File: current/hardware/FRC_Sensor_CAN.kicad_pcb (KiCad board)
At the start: 4 copper layers, 52 x 74 mm, 144 parts, among them J1 2P PUSH 3.5mm, J2 2P PUSH 3.5mm, J3 2P PUSH 3.5mm, J4 3P PUSH 3.5mm, J5 3P PUSH 3.5mm, J6 3P PUSH 3.5mm, J8 2x5 SERVICE SOCKET 2.54mm, Q1 AO4485, Q101 AO3401A, Q102 BSS138BK, Q2 BSS138BK, Q201 AO3401A, Q202 BSS138BK, Q3 BSS138BK, Q301 AO3401A, Q302 BSS138BK, U1 LMR51420XDDCR, U10 SN74AHCT1G125, U2 AP2112K-3.3, U4 TPS2553DBVR-1, U5 STM32F042K6T6, U6 TCAN3413DR, U7 LM339LV, U8 TPS61085DGKR, U9 TPS259620DDAR, Y1 8MHz 18pF

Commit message: Prepare factory SMT assembly with high-reflow C1 and exact MCU sourcing
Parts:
- C1: footprint FRC_Sensor_CAN:CP_Elec_8x6.5 -> FRC_Sensor_CAN:CP_Panasonic_FT_6.3x5.8

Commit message: Improve crystal startup margin and refresh pre-order verification
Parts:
- C25, C26: value 30pF -> 20pF
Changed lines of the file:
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@@
 			)
 		)
-		(property "Value" "30pF"
+		(property "Value" "20pF"
 			(at 0 1.68 90)
 			(layer "F.Fab")
@@
 			)
 		)
-		(property "MPN" "CC0805JRNPO9BN300"
+		(property "MPN" "CC0805JRNPO9BN200"
 			(at 0 0 0)
 			(layer "F.SilkS")
@@
 			)
 		)
-		(property "Value" "30pF"
+		(property "Value" "20pF"
 			(at 0 1.68 270)
 			(layer "F.Fab")
@@
 			)
 		)
-		(property "MPN" "CC0805JRNPO9BN300"
+		(property "MPN" "CC0805JRNPO9BN200"
 			(at 0 0 0)
 			(layer "F.SilkS")

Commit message: Snapshot current Rev H design for isolated compact-board work
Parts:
- L1: value 10uH -> 8.2uH
- U1: value LMR51420XDDCR -> LMR51430XDDCR
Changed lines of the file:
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@@
 			)
 		)
-		(property "Value" "LMR51420XDDCR"
+		(property "Value" "LMR51430XDDCR"
 			(at 0 2.4 180)
 			(layer "F.Fab")
@@
 			)
 		)
-		(property "MPN" "LMR51420XDDCR"
+		(property "MPN" "LMR51430XDDCR"
 			(at 0 0 0)
 			(layer "F.SilkS")
@@
 			)
 		)
-		(property "Value" "10uH"
+		(property "Value" "8.2uH"
 			(at 0 4.5 0)
 			(layer "F.Fab")
@@
 			)
 		)
-		(property "MPN" "SRP7028A-100M"
+		(property "MPN" "SRP7028A-8R2M"
 			(at 0 0 0)
 			(layer "F.SilkS")
@@
 			)
 		)
-		(property "Notes" "3.5A RMS, 6A saturation; use specified family, not NRND SRP7030."
+		(property "Notes" "4A RMS, 7.5A saturation; paired with 3A LMR51430. Use specified SRP7028A family."
 			(at 0 0 0)
 			(layer "F.SilkS")

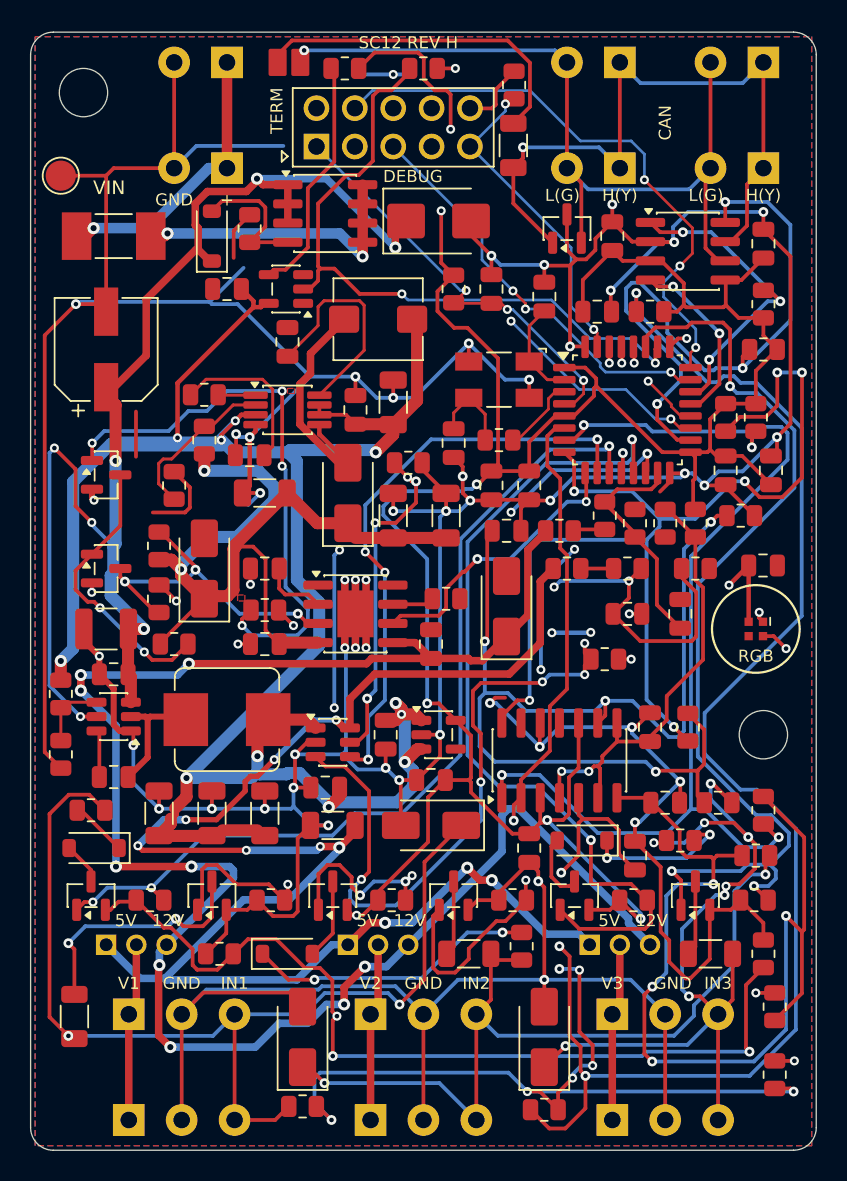
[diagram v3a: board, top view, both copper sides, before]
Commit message: Compact Rev H PCB to 52 x 70 mm with verified two-sided layout
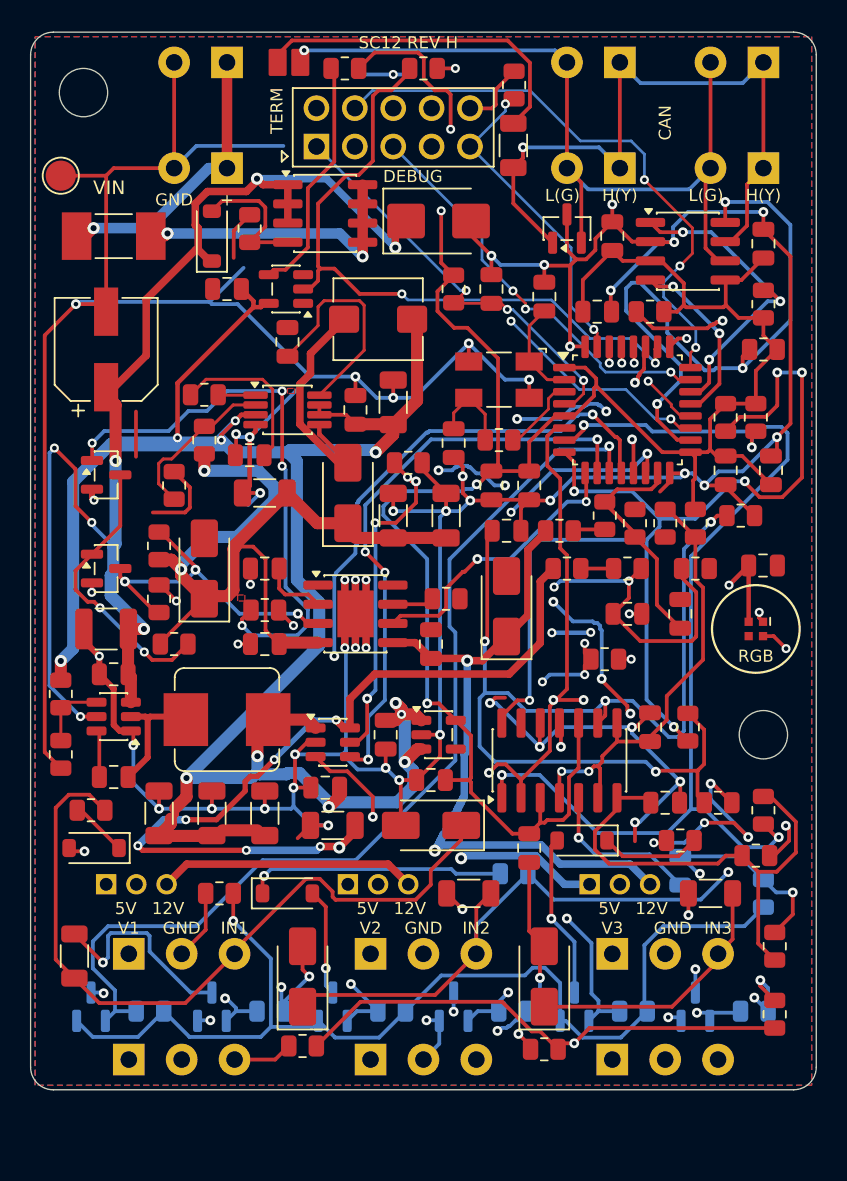
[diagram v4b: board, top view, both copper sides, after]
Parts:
- C101, Q101, Q102, Q201, Q202, Q301, Q302, R111, R112, R210, R211, R212, R311, R312, R52: moved to B.Cu
- moved Q101 7.35 mm to (4.00, 64.5)
- moved Q102 7.35 mm to (12.0, 64.5)
- moved Q201 7.35 mm to (20.0, 64.5)
- moved Q202 7.35 mm to (28.0, 64.5)
- moved Q301 7.35 mm to (36.0, 64.5)
- moved Q302 7.35 mm to (44.0, 64.5)
- moved R111 7.35 mm to (7.90, 64.8), turned to 180 degrees
- moved R112 7.35 mm to (15.9, 64.8), turned to 180 degrees
- moved R211 7.35 mm to (23.9, 64.8), turned to 180 degrees
- moved R212 7.35 mm to (31.9, 64.8), turned to 180 degrees
- moved R311 7.35 mm to (39.9, 64.8), turned to 180 degrees
- moved R312 7.35 mm to (47.9, 64.8), turned to 180 degrees
- moved R210 4.83 mm to (32.0, 55.7), turned to 0 degrees
- moved R109 4.00 mm to (2.90, 61.1)
- moved D201 4.00 mm to (18.0, 62.5)
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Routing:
- net GND: track 491.8 -> 422.6 mm, vias 60 -> 68
- net SENSOR_12V: track 120.2 -> 65.9 mm, vias 9 -> 2
- net INPUT1: track 132.2 -> 99.3 mm, vias 4 -> 5
- net SENSE2: track 63.2 -> 32.5 mm, vias 4 -> 0
- net SENSOR_5V: track 108.2 -> 79.6 mm, vias 10 -> 8
- net BIAS_UP2_N: track 46.9 -> 69.2 mm, vias 6 -> 3
- net POWER_5V_EN: track 66.9 -> 51.2 mm, vias 6 -> 5
- net SENSE1: track 71.5 -> 58.0 mm, vias 8 -> 2
- net BIAS_UP3_N: track 56.6 -> 45.1 mm
- net BIAS_SOURCE1: track 2.81 -> 11.9 mm, vias 0 -> 2
- net SIG1: track 68.2 -> 60.6 mm, vias 2 -> 0
- net SIG3: track 55.7 -> 48.2 mm, vias 8 -> 4
- net BIAS_SOURCE3: track 4.47 -> 10.9 mm, vias 0 -> 1
- net BIAS_UP1_N: track 59.3 -> 65.4 mm, vias 3 -> 1
- net BIAS_DOWN1: track 60.5 -> 66.0 mm, vias 4 -> 2
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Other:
- board size 52 x 74 mm -> 52 x 70 mm

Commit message: Shrink compact PCB to 44 x 48 mm and refresh verified outputs
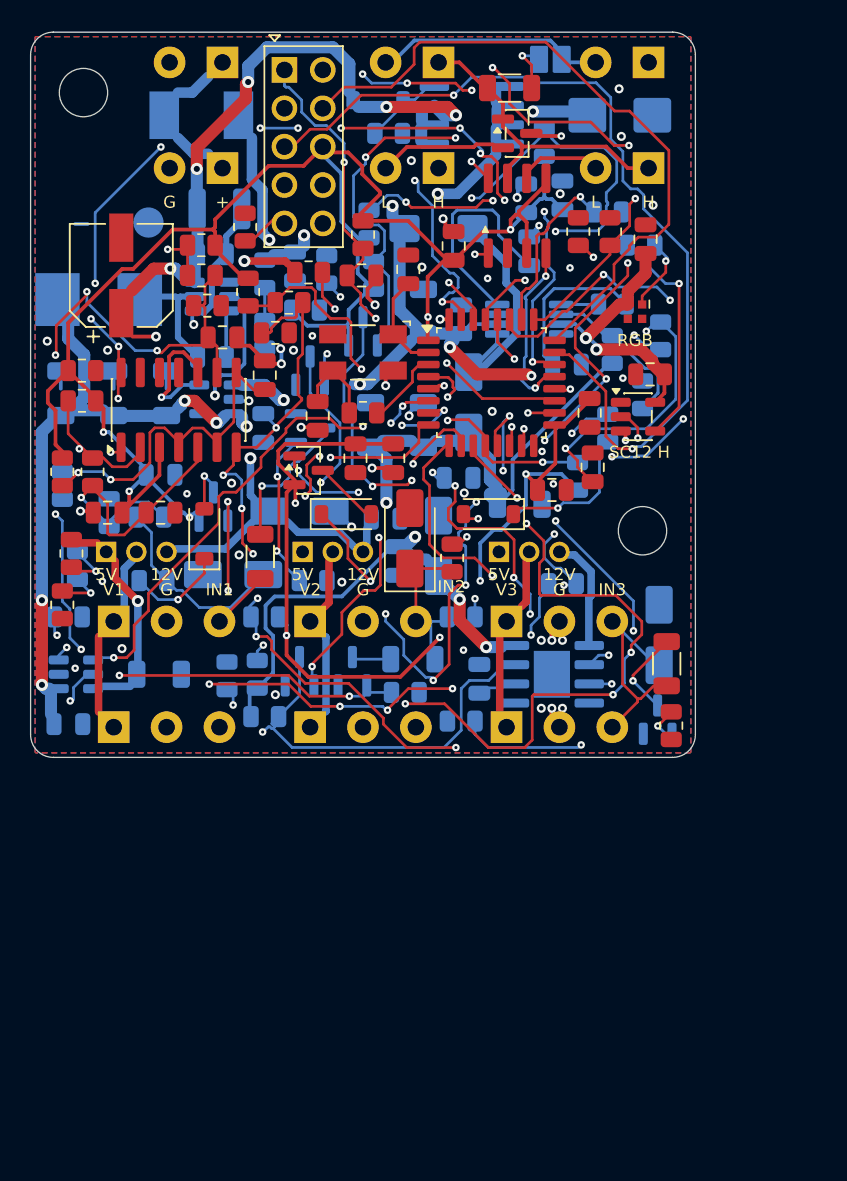
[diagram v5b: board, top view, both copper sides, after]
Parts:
- C101, Q201, R312, R52: moved to F.Cu
- C11, C12, C13, C2, C201, C3, C4, C40, C41, C5, C6, C60, C61, C62, C63, C64, C65, C66, C69, C7, C70, C71, C73, C8, D101, D2, D3, D301, D4, D5, D6, F1, JP2, L1, L2, Q1, Q2, Q3, R1, R10, R101, R103, R110, R2, R209, R3, R30, R301, R31, R310, R4, R40, R41, R51, R60, R61, R62, R63, R66, R68, R69, R70, R73, R75, TP1, U1, U2, U4, U8, U9: moved to B.Cu
- moved R52 56.8 mm to (3.40, 22.4), turned to 0 degrees
- moved R103 55.2 mm to (5.20, 31.8)
- moved R203 52.4 mm to (16.2, 19.9), turned to 0 degrees
- moved R311 51.6 mm to (22.7, 16.1), turned to 90 degrees
- moved R104 48.5 mm to (4.10, 29.1), turned to -90 degrees
- moved Q301 46.8 mm to (22.0, 19.8)
- moved R204 46.0 mm to (17.1, 17.9), turned to 0 degrees
- moved R304 43.9 mm to (11.3, 16.1), turned to 0 degrees
- moved R50 42.0 mm to (2.10, 29.1)
- moved R74 42.0 mm to (2.10, 37.9), turned to -90 degrees
- moved C101 41.8 mm to (8.60, 31.8), turned to 0 degrees
- moved R51 40.0 mm to (2.10, 30.0)
- moved R4 39.0 mm to (18.2, 18.4), turned to 0 degrees
- moved Q102 38.8 mm to (18.5, 26.2), turned to 0 degrees
- moved R105 38.1 mm to (3.40, 24.4)
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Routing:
- net GND: track 422.6 -> 32.2 mm, vias 68 -> 49
- net V5_INTERNAL: track 172.4 -> 107.0 mm, vias 14 -> 13
- net INPUT1: track 99.3 -> 37.7 mm
- net POWER_12V_EN: track 70.1 -> 17.7 mm, vias 5 -> 3
- net STATUS_DIN: track 53.6 -> 4.05 mm, vias 2 -> 1
- net SENSE2: track 32.5 -> 80.1 mm, vias 0 -> 9
- net BIAS_UP2_N: track 69.2 -> 22.6 mm, vias 3 -> 4
- net SENSOR_5V: track 79.6 -> 34.7 mm, vias 8 -> 1
- net SENSE1: track 58.0 -> 18.2 mm, vias 2 -> 1
- net ADC12_DIV: track 2.12 -> 40.0 mm, vias 0 -> 2
- net +3V3: track 237.0 -> 199.6 mm, vias 4 -> 12
- net POWER_5V_EN: track 51.2 -> 88.5 mm, vias 5 -> 4
- net SIG2: track 53.6 -> 16.7 mm, vias 2 -> 0
- net SIG1: track 60.6 -> 23.9 mm
- net BIAS_DOWN2: track 56.9 -> 89.2 mm, vias 2 -> 9
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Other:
- board size 52 x 70 mm -> 44 x 48 mm
- board text added: "G"
- board text added: "H"
- board text added: "L"
- board text added: "SC12 H"
- board text added: "sugarCANe"
- board text removed: "CAN"
- board text removed: "DEBUG"
- board text removed: "H(Y)"
- board text removed: "L(G)"
- board text removed: "SC12 REV H"
- board text removed: "VIN"

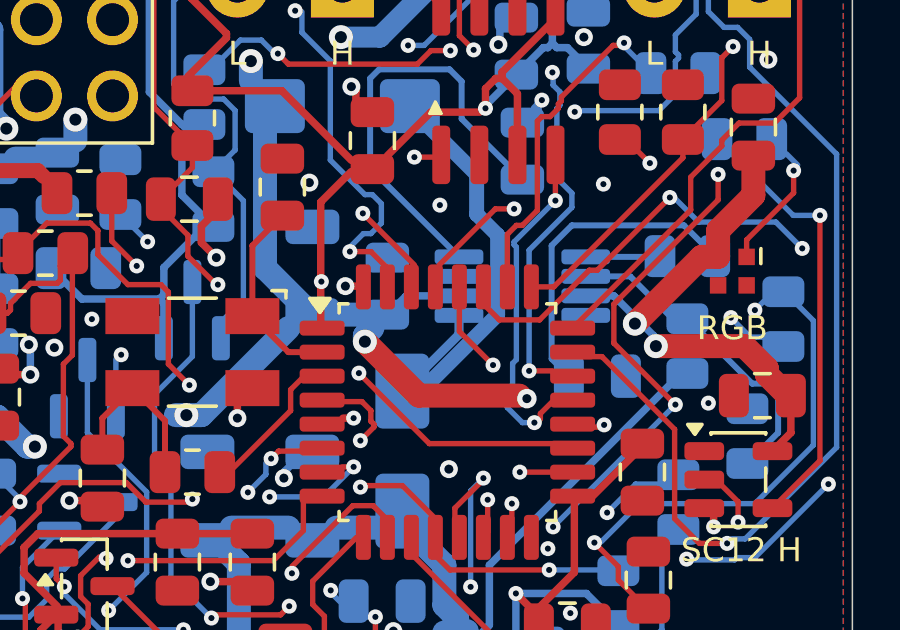
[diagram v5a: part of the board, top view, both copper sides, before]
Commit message: Fix U8 switch-node pad corner contact on compact board
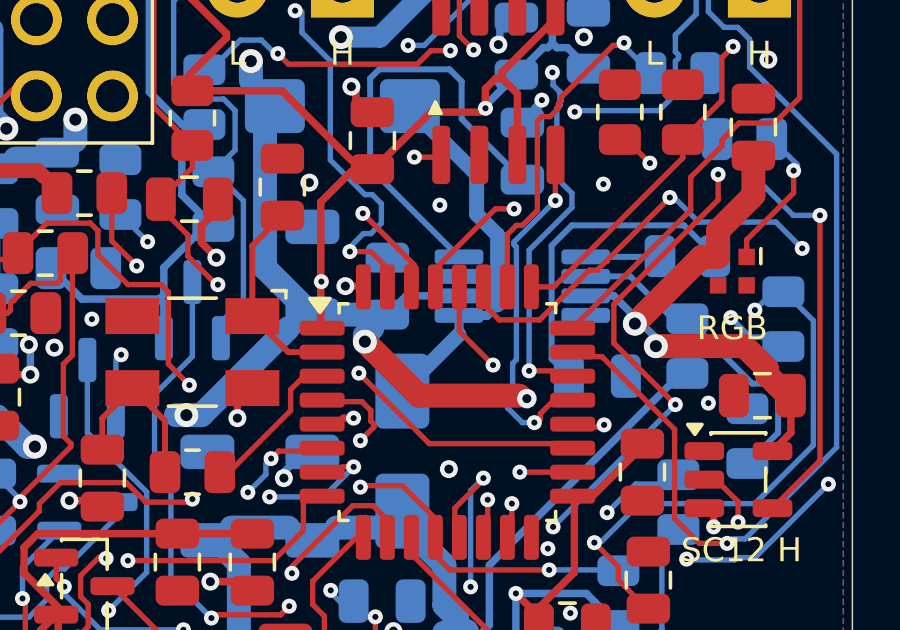
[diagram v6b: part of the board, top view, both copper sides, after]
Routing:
- net BOOST_SW: track 14.8 -> 12.1 mm
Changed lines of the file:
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@@
+	)
+	(segment
+		(start 31.825 19.975)
+		(end 30.8875 19.975)
+		(width 0.3)
+		(layer "B.Cu")
+		(net "BOOST_SW")
 	)
 	(segment
 		(start 29 22.5)
 		(end 30.8875 20.6125)
-		(width 0.3)
+		(width 0.5)
 		(locked yes)
 		(layer "B.Cu")
@@
 	)
 	(segment
-		(start 29.5 22.625)
-		(end 32.175 19.95)
-		(width 0.5)
+		(start 32.175 19.625)
+		(end 31.825 19.975)
+		(width 0.3)
 		(locked yes)
 		(layer "B.Cu")
@@
 	)
 	(segment
-		(start 32.175 19.95)
+		(start 32.175 19.625)
 		(end 32.175 17.3)
 		(width 0.5)
@@
 		(polygon
 			(pts
-				(xy 29.812012 12.63209) (xy 29.671317 12.589411) (xy 29.525 12.575) (xy 29.378682 12.589411) (xy 29.237987 12.63209)
-				(xy 29.108322 12.701397) (xy 28.994669 12.794669) (xy 28.901397 12.908322) (xy 28.83209 13.037987)
-				(xy 28.789411 13.178682) (xy 28.775 13.325) (xy 28.789411 13.471317) (xy 28.83209 13.612012) (xy 28.901397 13.741677)
-				(xy 28.994669 13.85533) (xy 30.725 15.58566) (xy 30.725 16.599999) (xy 30.725 16.6) (xy 30.739411 16.746317)
-				(xy 30.78209 16.887012) (xy 30.851397 17.016677) (xy 30.944669 17.13033) (xy 31.424999 17.61066)
-				(xy 31.424999 19.610278) (xy 31.347119 19.51538) (xy 31.24862 19.434544) (xy 31.136244 19.374478)
-				(xy 31.014308 19.337489) (xy 30.8875 19.325) (xy 30.760691 19.337489) (xy 30.638755 19.374478) (xy 30.526379 19.434544)
-				(xy 30.42788 19.51538) (xy 30.347044 19.613879) (xy 30.286978 19.726255) (xy 30.249989 19.848191)
-				(xy 30.2375 19.975) (xy 30.2375 20.343261) (xy 28.54038 22.04038) (xy 28.459544 22.138879) (xy 28.399478 22.251255)
-				(xy 28.362489 22.373191) (xy 28.35 22.5) (xy 28.362489 22.626808) (xy 28.399478 22.748744) (xy 28.459544 22.86112)
-				(xy 28.54038 22.959619) (xy 28.638879 23.040455) (xy 28.751255 23.100521) (xy 28.873191 23.13751)
-				(xy 28.962243 23.146281) (xy 28.969669 23.15533) (xy 29.083322 23.248602) (xy 29.212987 23.317909)
-				(xy 29.353682 23.360588) (xy 29.5 23.375) (xy 29.646317 23.360588) (xy 29.787012 23.317909) (xy 29.916677 23.248602)
-				(xy 30.03033 23.15533) (xy 32.70533 20.48033) (xy 32.798602 20.366677) (xy 32.867909 20.237012)
-				(xy 32.910588 20.096317) (xy 32.924999 19.95) (xy 32.924999 17.3) (xy 32.910588 17.153682) (xy 32.867909 17.012987)
-				(xy 32.798602 16.883322) (xy 32.760328 16.836686) (xy 32.70533 16.769669) (xy 32.225 16.289339)
-				(xy 32.225 15.275) (xy 32.210588 15.128682) (xy 32.167909 14.987987) (xy 32.098602 14.858322) (xy 32.00533 14.744669)
-				(xy 30.05533 12.794669) (xy 29.941677 12.701397)
-			)
-		)
+				(xy 29.941677 12.701397) (xy 29.941671 12.701394) (xy 29.878548 12.663559) (xy 29.812013 12.632091)
+				(xy 29.812012 12.63209) (xy 29.812009 12.632089) (xy 29.742714 12.607295) (xy 29.671318 12.589411)
+				(xy 29.598513 12.578611) (xy 29.525 12.575) (xy 29.451487 12.578611) (xy 29.378684 12.589411) (xy 29.378682 12.589411)
+				(xy 29.37868 12.589412) (xy 29.307286 12.607295) (xy 29.237996 12.632087) (xy 29.237987 12.63209)
+				(xy 29.237978 12.632095) (xy 29.171452 12.663559) (xy 29.108337 12.701389) (xy 29.108322 12.701397)
+				(xy 29.108309 12.701408) (xy 29.049205 12.745242) (xy 28.994689 12.794652) (xy 28.994669 12.794669)
+				(xy 28.994652 12.794689) (xy 28.945242 12.849205) (xy 28.901408 12.908309) (xy 28.901397 12.908322)
+				(xy 28.901389 12.908337) (xy 28.863559 12.971452) (xy 28.832095 13.037978) (xy 28.83209 13.037987)
+				(xy 28.832087 13.037996) (xy 28.807295 13.107286) (xy 28.789412 13.17868) (xy 28.789411 13.178682)
+				(xy 28.789411 13.178684) (xy 28.778611 13.251487) (xy 28.775 13.325) (xy 28.778611 13.398513) (xy 28.789411 13.471318)
+				(xy 28.807295 13.542714) (xy 28.832089 13.612009) (xy 28.83209 13.612012) (xy 28.832091 13.612013)
+				(xy 28.863559 13.678548) (xy 28.901394 13.741671) (xy 28.901397 13.741677) (xy 28.9014 13.741681)
+				(xy 28.945242 13.800795) (xy 28.994661 13.85532) (xy 28.994669 13.85533) (xy 30.427764 15.288424)
+				(xy 30.725 15.58566) (xy 30.725 16.599999) (xy 30.725 16.6) (xy 30.728611 16.673513) (xy 30.739411 16.746318)
+				(xy 30.757295 16.817714) (xy 30.782089 16.887009) (xy 30.78209 16.887012) (xy 30.782091 16.887013)
+				(xy 30.813559 16.953548) (xy 30.851394 17.016671) (xy 30.851397 17.016677) (xy 30.8514 17.016681)
+				(xy 30.895242 17.075795) (xy 30.944661 17.13032) (xy 30.944669 17.13033) (xy 31.424999 17.61066)
+				(xy 31.424999 19.325) (xy 30.8875 19.325) (xy 30.823789 19.32813) (xy 30.760703 19.337488) (xy 30.760691 19.337489)
+				(xy 30.760679 19.337493) (xy 30.698815 19.352989) (xy 30.638766 19.374475) (xy 30.638755 19.374478)
+				(xy 30.638744 19.374484) (xy 30.581092 19.401751) (xy 30.526394 19.434536) (xy 30.526379 19.434544)
+				(xy 30.526366 19.434554) (xy 30.475144 19.472543) (xy 30.427893 19.515369) (xy 30.42788 19.51538)
+				(xy 30.427869 19.515393) (xy 30.385043 19.562644) (xy 30.347054 19.613866) (xy 30.347044 19.613879)
+				(xy 30.347036 19.613894) (xy 30.314251 19.668592) (xy 30.286984 19.726244) (xy 30.286978 19.726255)
+				(xy 30.286975 19.726266) (xy 30.265489 19.786315) (xy 30.249993 19.848179) (xy 30.249989 19.848191)
+				(xy 30.249988 19.848203) (xy 30.24063 19.911289) (xy 30.2375 19.975) (xy 30.2375 20.20184) (xy 28.46967 21.96967)
+				(xy 28.420242 22.024205) (xy 28.376398 22.083322) (xy 28.338559 22.146452) (xy 28.30709 22.212987)
+				(xy 28.282295 22.282286) (xy 28.264411 22.353682) (xy 28.253611 22.426487) (xy 28.25 22.5) (xy 28.253611 22.573513)
+				(xy 28.264411 22.646318) (xy 28.282295 22.717714) (xy 28.30709 22.787013) (xy 28.338559 22.853548)
+				(xy 28.376398 22.916678) (xy 28.420242 22.975795) (xy 28.46967 23.03033) (xy 28.524205 23.079758)
+				(xy 28.583322 23.123602) (xy 28.646452 23.161441) (xy 28.712987 23.19291) (xy 28.782286 23.217705)
+				(xy 28.853682 23.235589) (xy 28.926487 23.246389) (xy 29 23.25) (xy 29.073513 23.246389) (xy 29.079536 23.245495)
+				(xy 29.083322 23.248602) (xy 29.212987 23.317909) (xy 29.353682 23.360588) (xy 29.5 23.375) (xy 29.646317 23.360588)
+				(xy 29.787012 23.317909) (xy 29.916677 23.248602) (xy 30.03033 23.15533) (xy 32.70533 20.48033)
+				(xy 32.798602 20.366677) (xy 32.867909 20.237012) (xy 32.910588 20.096317) (xy 32.924999 19.95)
+				(xy 32.924999 19.62502) (xy 32.925 19.625) (xy 32.925 17.3) (xy 32.921389 17.226487) (xy 32.910589 17.153682)
+				(xy 32.892705 17.082286) (xy 32.86791 17.012987) (xy 32.836441 16.946452) (xy 32.798602 16.883322)
+				(xy 32.754758 16.824205) (xy 32.705337 16.769678) (xy 32.70533 16.769669) (xy 32.225 16.289339)
+				(xy 32.225 15.275) (xy 32.221389 15.201487) (xy 32.210589 15.128682) (xy 32.192705 15.057286) (xy 32.16791 14.987987)
+				(xy 32.136441 14.921452) (xy 32.098602 14.858322) (xy 32.054758 14.799205) (xy 32.005337 14.744678)
+				(xy 32.00533 14.744669) (xy 30.05533 12.794669) (xy 30.05532 12.794661) (xy 30.000795 12.745242)
+				(xy 29.941681 12.7014)
+			)
+		)

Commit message: Add local boost ground return and document compact simulation scope
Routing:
- net GND: vias 49 -> 50
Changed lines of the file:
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@@
+	)
+	(via
+		(at 36.2 22.85)
+		(size 0.5)
+		(drill 0.2)
+		(layers "F.Cu" "B.Cu")
+		(net "GND")
 	)
 	(via
